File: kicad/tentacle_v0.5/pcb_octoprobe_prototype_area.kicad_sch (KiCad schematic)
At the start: 14 parts, among them J1302 Conn_02x20, J1303 Conn_02x20

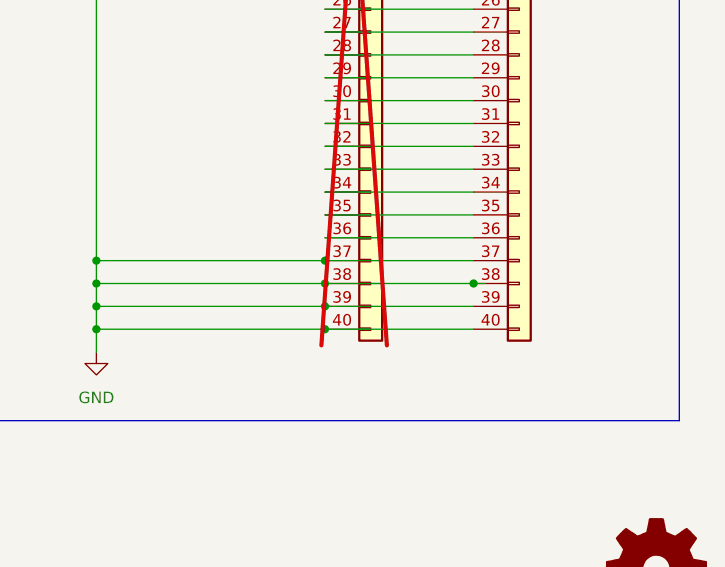
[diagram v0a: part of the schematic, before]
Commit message: Schematics: Fix ERC warnings
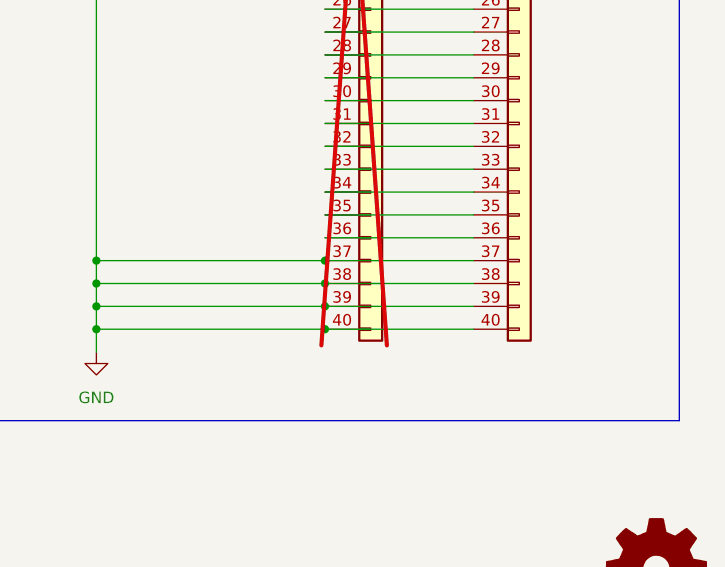
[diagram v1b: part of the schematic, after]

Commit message: Breadboard: Remove pads from schematic
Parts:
- removed BP1301: prototype_GND, 00_project_library:octoprobe_breakout_PB, symbol 00_project_library:octoprobe_breakout_BP
- removed BP1302: prototype_NC, 00_project_library:octoprobe_breakout_PB_NC, symbol 00_project_library:octoprobe_breakout_PB_NC
- removed H1301, H1302, H1303, H1304: octoprobe_CableTieHole, 00_project_library:octoprobe_CableTieHole, symbol 00_project_library:octoprobe_CableTieHole
